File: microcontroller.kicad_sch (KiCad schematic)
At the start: 41 parts, among them J1 USB4105-GF-A, J2 LEFT, J3 RIGHT, J4 DEBUG, U1 RP2354A, U2 MCP1702T-3302E_CB, X1 IQXO-791_12MHz

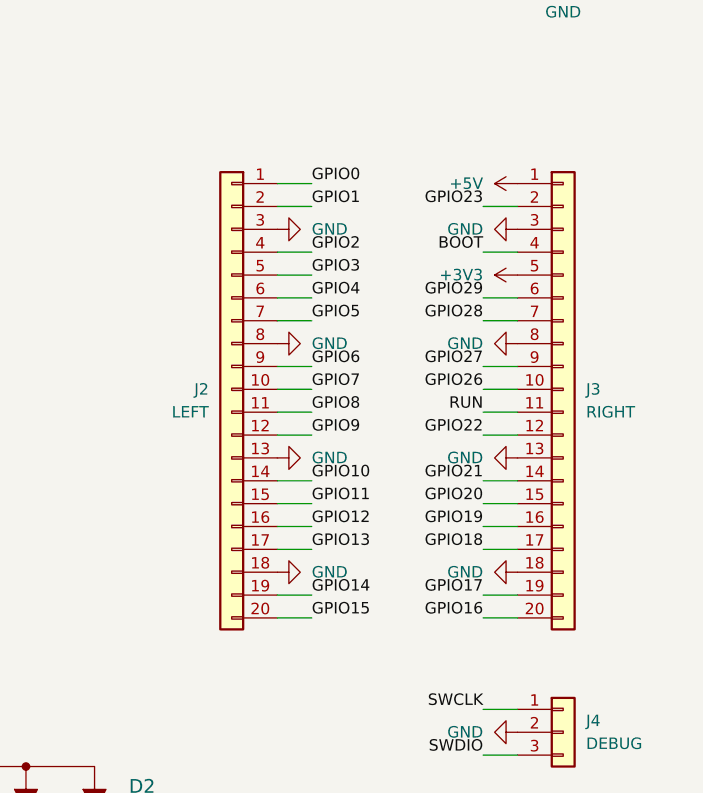
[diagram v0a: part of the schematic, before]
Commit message: Delete Header Pins
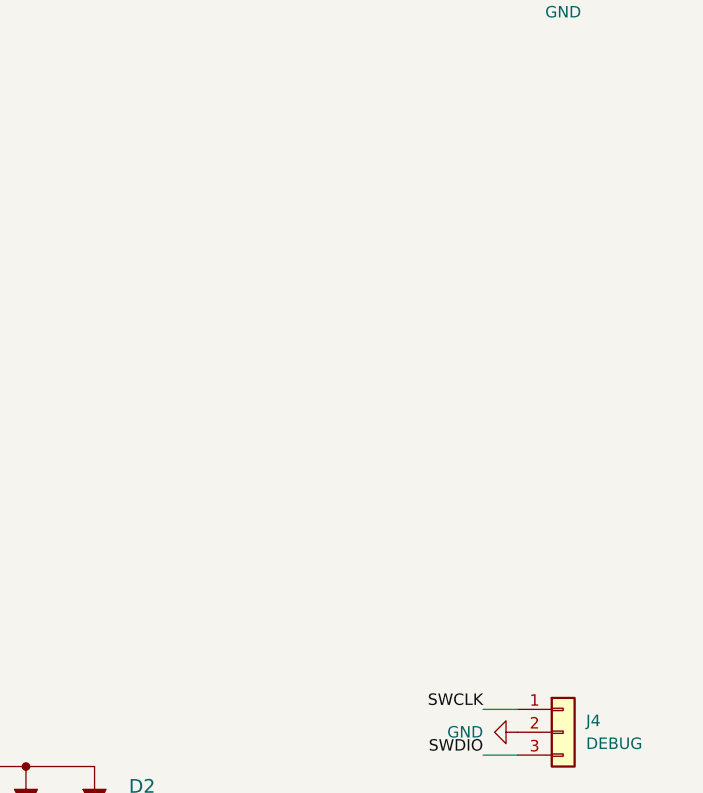
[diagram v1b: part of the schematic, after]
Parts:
- removed J2: LEFT, Connector_PinHeader_2.54mm:PinHeader_1x20_P2.54mm_Vertical, symbol Connector_Generic:Conn_01x20
- removed J3: RIGHT, Connector_PinHeader_2.54mm:PinHeader_1x20_P2.54mm_Vertical, symbol Connector_Generic:Conn_01x20

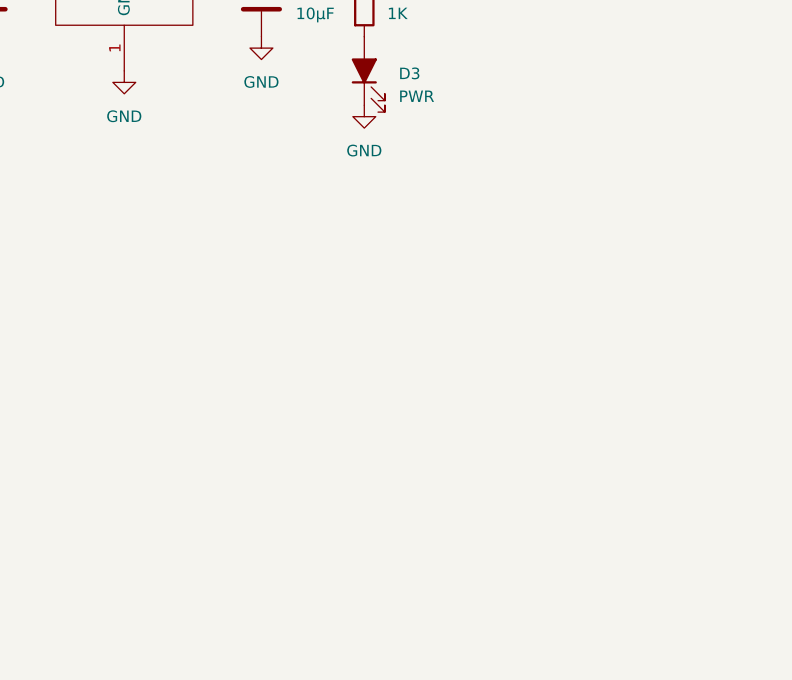
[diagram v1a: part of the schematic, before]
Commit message: finished output and added sd card
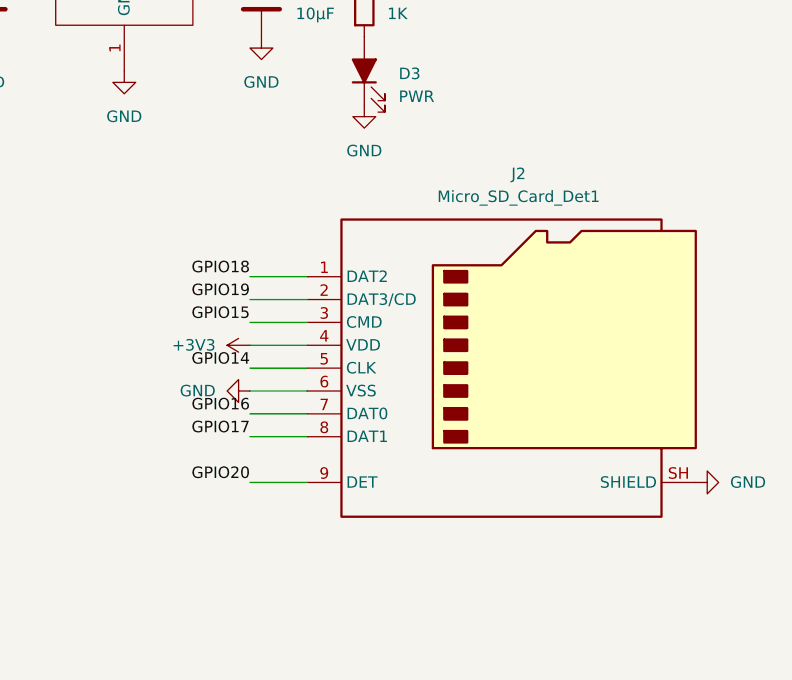
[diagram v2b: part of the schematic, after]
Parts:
- added J2: Micro_SD_Card_Det1, symbol Connector:Micro_SD_Card_Det1
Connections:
- net +3V3: now also J2.4 (VDD)
- net GND: now also J2.6 (VSS), J2.SH (SHIELD)
- net GPIO14: now also J2.5 (CLK)
- net GPIO15: now also J2.3 (CMD)
- net GPIO16: now also J2.7 (DAT0)
- net GPIO17: now also J2.8 (DAT1)
- net GPIO18: now also J2.1 (DAT2)
- net GPIO19: now also J2.2 (DAT3/CD)
- net GPIO20: now also J2.9 (DET)
